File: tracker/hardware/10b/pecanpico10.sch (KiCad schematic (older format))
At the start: 121 parts, among them IC1 SPV1040T, IC10 AS213-92LF, IC2 TPS62260DRVR, IC3 ADP322ACPZ-115-R7, IC4 Si4464-B1B-FM, IC5 STM32F413RHT6, IC6 EVA-7M or EVA-M8, IC7 PAC1720-1-AIA-TR, IC8 TPS62260DRVR, IC9 BME280, J1 DM3AT-SF-PEJM5, J2 CONN_01X15, P1 CONN_01X25, P3 ZX62-B-5PA(33), P4 SMA, Q1 FDN306P, X1 KT2016K26000BCW18ZAS

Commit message: Fixed USB/battery isolation bug, increased schottky diode pad size
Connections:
- net +BATT: now also Q1.2 (S)
- net BATT_CONN: no longer names the net of J2.3 (P3), W11.1
- net BATT_CONN: no longer Q1.2 (S)
- net IO_RXD renamed IO_RXD_SDA
- net IO_TXD renamed IO_TXD_SCL
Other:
- note added: "Conect solar cells\nbetween pin 1 and 2"
- note added: "Connect pin 13 and 14 to get\ninto the STM bootloader"
- note added: "Connect pin 3 and 4 with a\njumper in order to connect\nthe battery with the circuit"
- note added: "Pin 12: Pin for general purpose"
- note added: "Pin 6 and 7 can be either\nused for UART or I2C"
- note added: "Pin 8-11: SWD interface"
- note added: "Solder the battery\nto those pads\n(either LiPO or\n3x L92 batteries)"
- moved on the sheet: D1, J2, Q1, R16, R31, W1, W10, W11

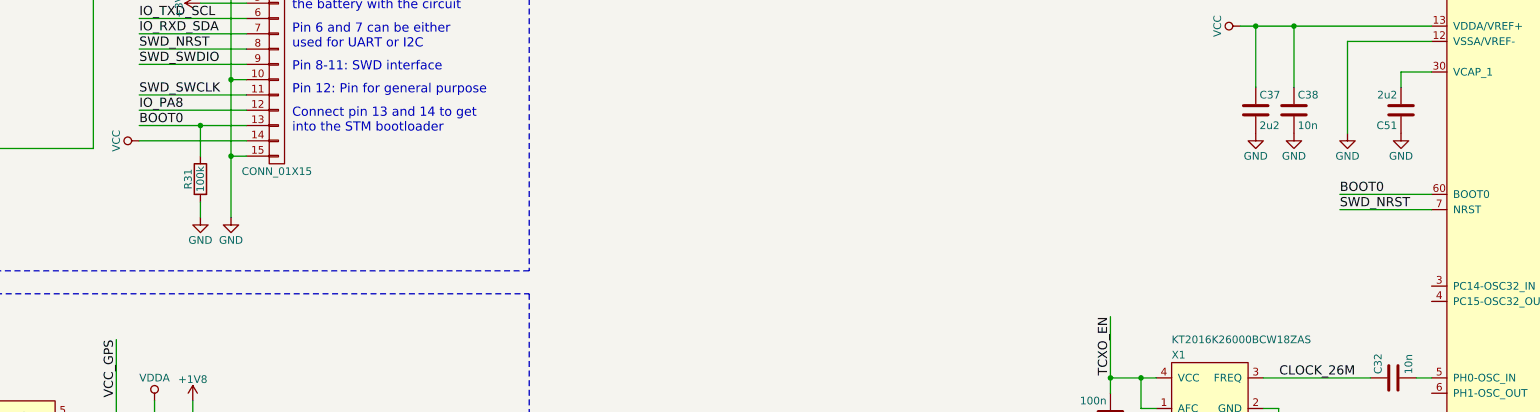
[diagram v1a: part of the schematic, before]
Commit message: Added one more pin to pinheader
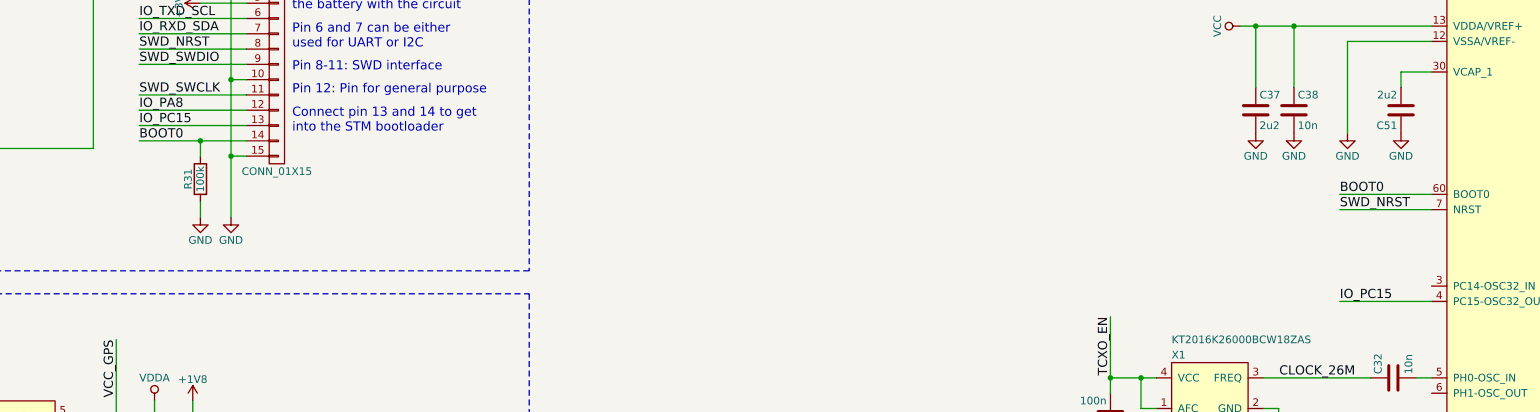
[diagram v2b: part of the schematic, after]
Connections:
- net BOOT0: now also J2.14 (P14); no longer J2.13 (P13)
- net VCC: no longer J2.14 (P14)
- net IO_PC15: now reaches IC5.4 (PC15-OSC32_OUT)
- net IO_PC15: now also J2.13 (P13)
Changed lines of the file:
@@
 Text Label 15800 5100 0    60   ~ 0
 BOOT0
-Text Label 7950 4650 0    60   ~ 0
+Text Label 7950 4750 0    60   ~ 0
 BOOT0
 $Comp
@@
 	1    0    0    -1
 $EndComp
-$Comp
-L VCC #PWR0102
-U 1 1 5A304A3C
-P 7950 4750
-F 0 "#PWR0102" H 7950 4600 50  0001 C CNN
-F 1 "VCC" H 7950 4900 50  0000 C CNN
-F 2 "" H 7950 4750 50  0001 C CNN
-F 3 "" H 7950 4750 50  0001 C CNN
-	1    7950 4750
-	0    -1   -1   0
-$EndComp
 Text Notes 1300 8050 0    60   ~ 0
 Power and Voltage sensing
 $Comp
-L +3V3 #PWR0103
+L +3V3 #PWR0102
 U 1 1 5A319E64
 P 14350 14150
-F 0 "#PWR0103" H 14350 14000 50  0001 C CNN
+F 0 "#PWR0102" H 14350 14000 50  0001 C CNN
 F 1 "+3V3" H 14350 14290 50  0000 C CNN
 F 2 "" H 14350 14150 50  0000 C CNN
@@
 $EndComp
 $Comp
-L +1V8 #PWR0104
+L +1V8 #PWR0103
 U 1 1 5A31B091
 P 11900 14000
-F 0 "#PWR0104" H 11900 13850 50  0001 C CNN
+F 0 "#PWR0103" H 11900 13850 50  0001 C CNN
 F 1 "+1V8" H 11900 14140 50  0000 C CNN
 F 2 "" H 11900 14000 50  0001 C CNN
@@
 $EndComp
 $Comp
-L +1V8 #PWR0105
+L +1V8 #PWR0104
 U 1 1 5A31B20B
 P 8300 6450
-F 0 "#PWR0105" H 8300 6300 50  0001 C CNN
+F 0 "#PWR0104" H 8300 6300 50  0001 C CNN
 F 1 "+1V8" H 8300 6590 50  0000 C CNN
 F 2 "" H 8300 6450 50  0001 C CNN
@@
 POWER BUSSES
 $Comp
-L VCC #PWR0106
+L VCC #PWR0105
 U 1 1 5A328681
 P 5900 3150
-F 0 "#PWR0106" H 5900 3000 50  0001 C CNN
+F 0 "#PWR0105" H 5900 3000 50  0001 C CNN
 F 1 "VCC" H 5900 3300 50  0000 C CNN
 F 2 "" H 5900 3150 50  0001 C CNN
@@
 $EndComp
 $Comp
-L GND #PWR0107
+L GND #PWR0106
 U 1 1 5A319B63
 P 9150 15050
-F 0 "#PWR0107" H 9150 14800 50  0001 C CNN
+F 0 "#PWR0106" H 9150 14800 50  0001 C CNN
 F 1 "GND" H 9150 14900 50  0000 C CNN
 F 2 "" H 9150 15050 50  0000 C CNN
@@
 $EndComp
 $Comp
-L GND #PWR0108
+L GND #PWR0107
 U 1 1 5A318389
 P 20100 7750
-F 0 "#PWR0108" H 20100 7500 50  0001 C CNN
+F 0 "#PWR0107" H 20100 7500 50  0001 C CNN
 F 1 "GND" H 20100 7600 50  0000 C CNN
 F 2 "" H 20100 7750 50  0001 C CNN
@@
 TCXO_EN
 $Comp
-L GND #PWR0109
+L GND #PWR0108
 U 1 1 5A3CF6C1
 P 7300 3650
-F 0 "#PWR0109" H 7300 3400 50  0001 C CNN
+F 0 "#PWR0108" H 7300 3400 50  0001 C CNN
 F 1 "GND" H 7300 3500 50  0000 C CNN
 F 2 "" H 7300 3650 50  0000 C CNN
@@
 	11900 12900 12900 12900
 Wire Wire Line
-	7950 4750 8650 4750
-Wire Wire Line
 	8450 3750 8650 3750
 Wire Wire Line
@@
 	18600 6750 19800 6750
 Wire Wire Line
-	7950 4650 8650 4650
-Wire Wire Line
 	6000 3150 5900 3150
 Wire Wire Line
@@
 Wire Wire Line
 	2800 12900 3500 12900
-Wire Wire Line
-	8350 4850 8350 4650
-Connection ~ 8350 4650
 Wire Wire Line
 	8350 5250 8350 5150
@@
 $EndComp
 $Comp
-L +BATT #PWR?
+L +BATT #PWR0109
 U 1 1 5AD41EDF
 P 7500 2600
-F 0 "#PWR?" H 7500 2450 50  0001 C CNN
+F 0 "#PWR0109" H 7500 2450 50  0001 C CNN
 F 1 "+BATT" H 7500 2740 50  0000 C CNN
 F 2 "" H 7500 2600 50  0000 C CNN
@@
 Wire Notes Line
 	4800 1500 10500 1500
+Wire Wire Line
+	7950 4750 8650 4750
+Wire Wire Line
+	8650 4650 7950 4650
+Text Label 7950 4650 0    60   ~ 0
+IO_PC15
+Text Label 15800 5800 0    60   ~ 0
+IO_PC15
+Wire Wire Line
+	15800 5800 16400 5800
+Wire Wire Line
+	8350 4850 8350 4750
+Connection ~ 8350 4750
 $EndSCHEMATC

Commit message: Relabeled pinheader
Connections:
- net IO_RXD_SDA renamed IO_RXD
- net IO_TXD_SCL renamed IO_TXD

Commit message: Fixed power measuring bug
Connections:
- net +BATT: no longer IC7.3 (SENSE2+), R22.1, R29.2
- net VDD: now also IC7.3 (SENSE2+), R22.1, R29.2; no longer C3.1, C4.2, C7.2, C8.1, C9.1, IC1.4 (VOUT), IC2.4 (EN), IC2.5 (VIN), IC3.10 (VIN3), IC3.2 (VBIAS), IC3.3 (VIN1/VIN2), IC7.4 (SENSE2-), IC8.4 (EN), IC8.5 (VIN), R1.1, R22.2, R30.2, R5.1
- new net SENSE_BAT-: C3.1, C4.2, C7.2, C8.1, C9.1, IC1.4 (VOUT), IC2.4 (EN), IC2.5 (VIN), IC3.10 (VIN3), IC3.2 (VBIAS), IC3.3 (VIN1/VIN2), IC7.4 (SENSE2-), IC8.4 (EN), IC8.5 (VIN), R1.1, R22.2, R30.2, R5.1
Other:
- moved on the sheet: C10, C11, C12, C8, C9, D4, IC3, R14, R15, R9

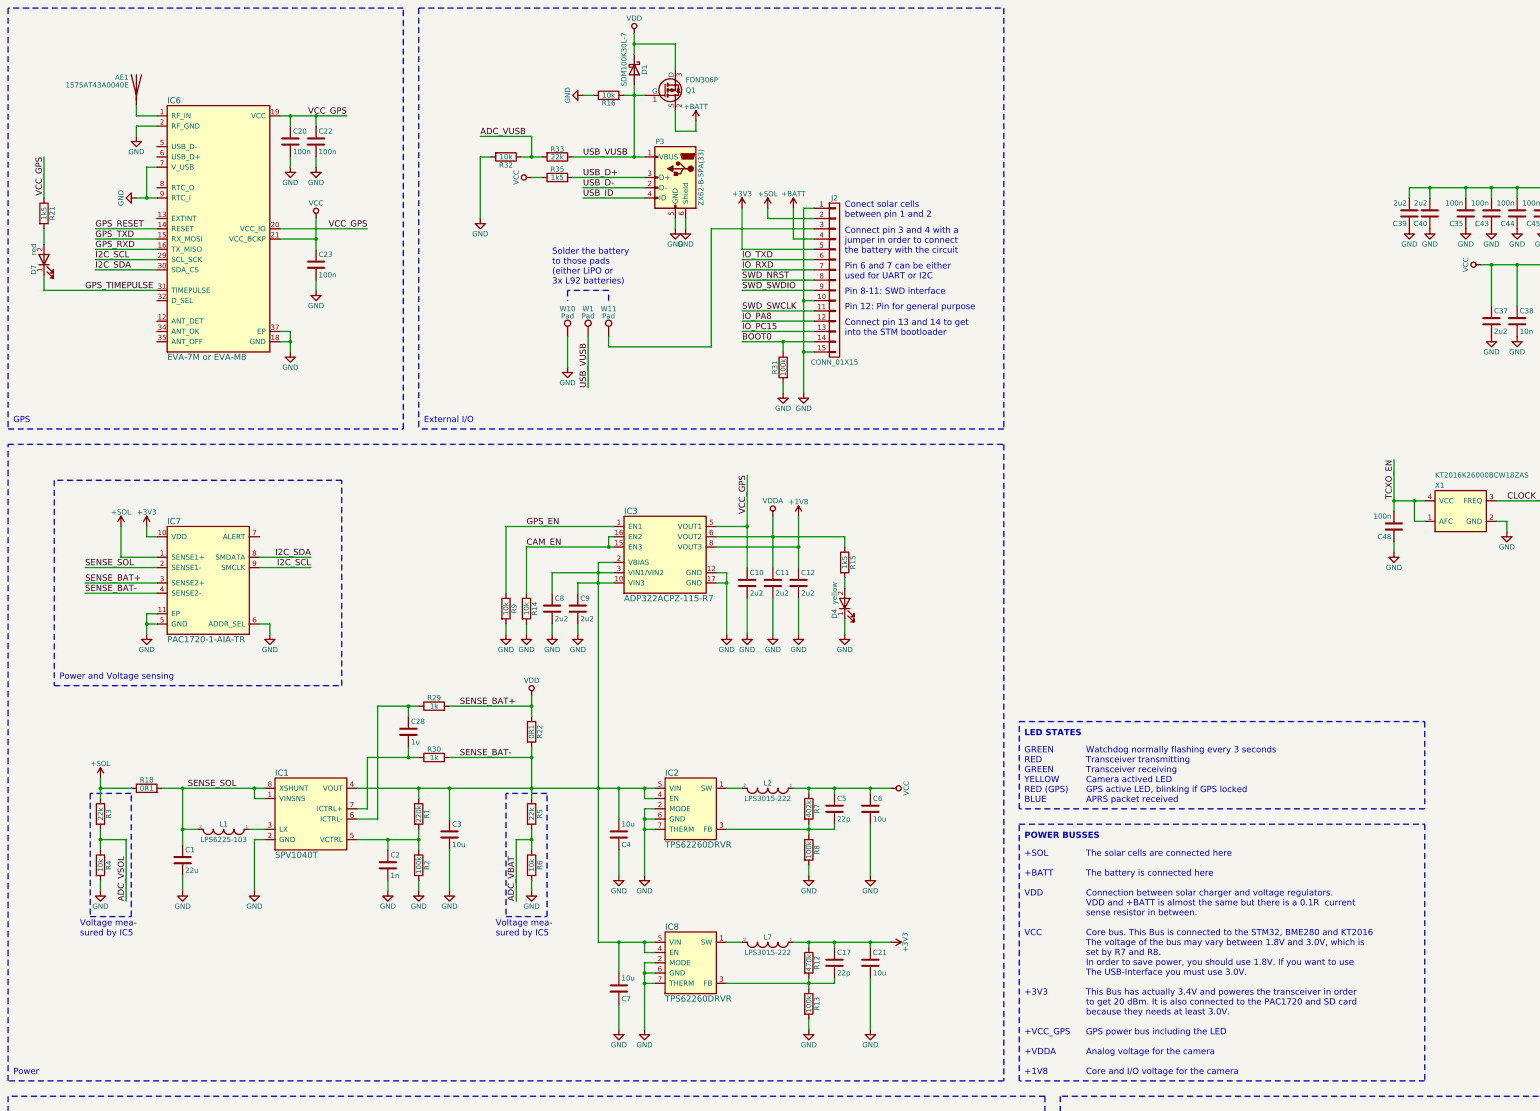
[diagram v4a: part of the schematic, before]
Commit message: Added 2m bandpass trap filter in GPS rx Removed unnecessary resistor Edited/Added schematic comments
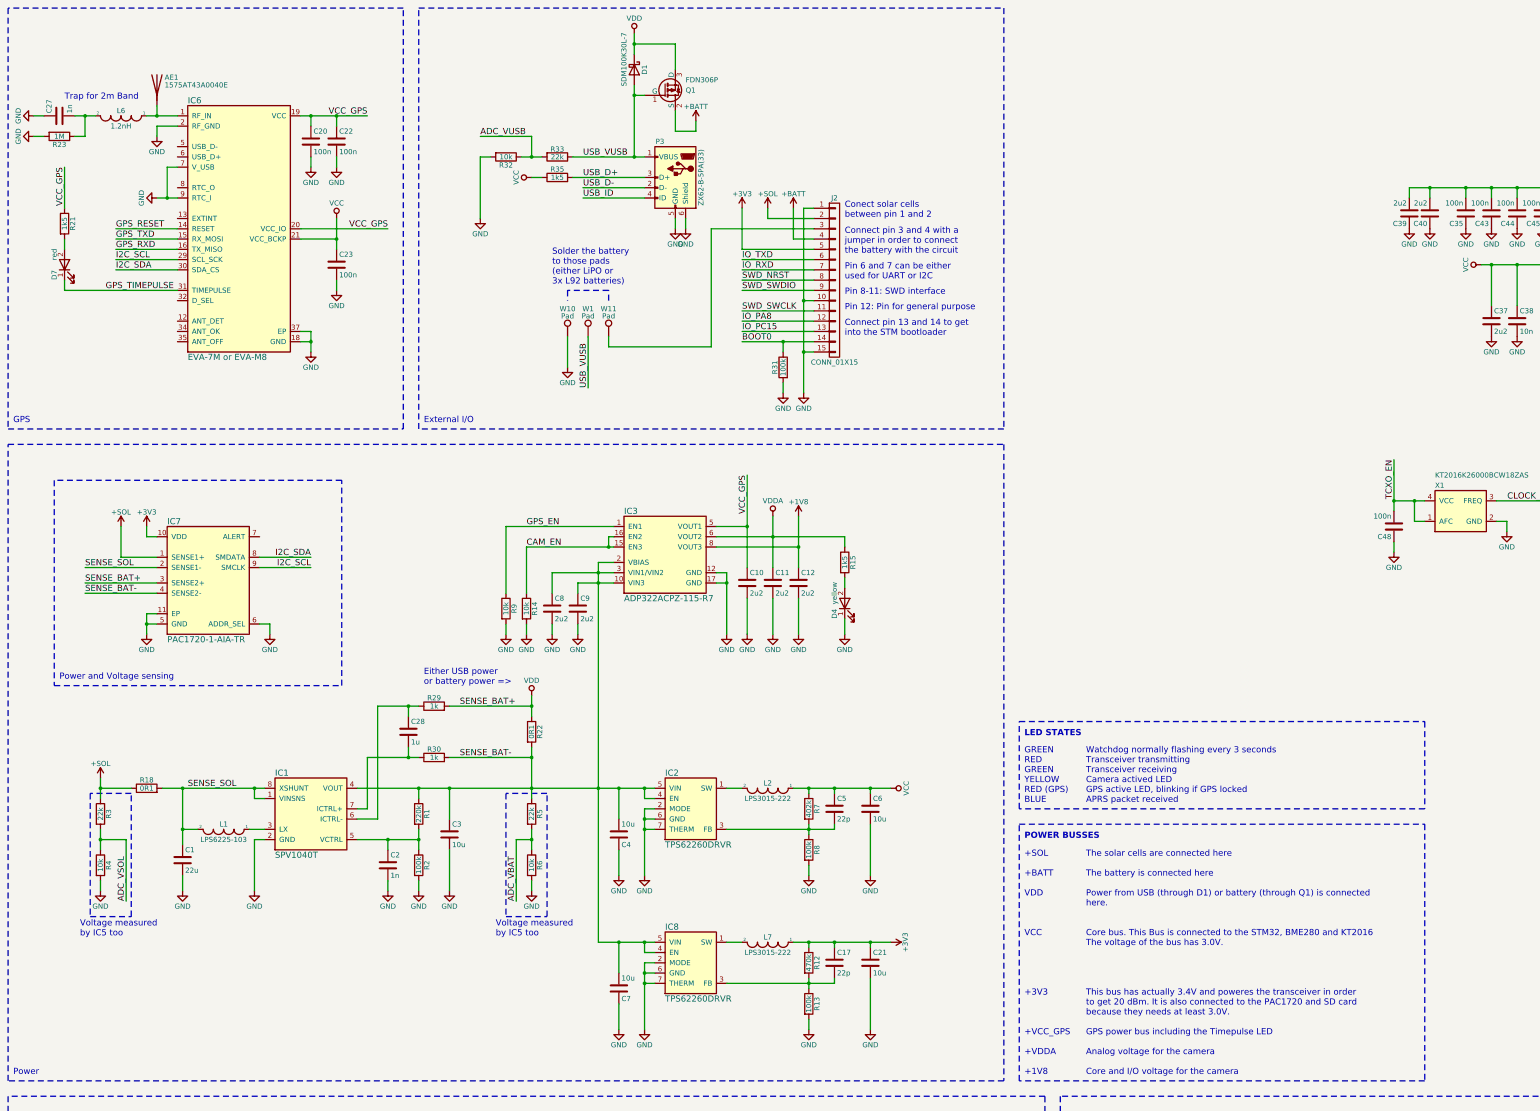
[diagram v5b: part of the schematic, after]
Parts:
- removed R16: 10k, pecanpico:R_0402, symbol R
- added C27: 1n, pecanpico:C_0402, symbol C
- added L6: 1.2nH, pecanpico:R_0603, symbol INDUCTOR
- added R23: 1M, pecanpico:R_0402, symbol R
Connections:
- net GND: now also C27.1, R23.2
- net at AE1.1 (A), IC6.1 (RF_IN): now also L6.1
- new net: C27.2, L6.2, R23.1
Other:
- note added: "Either USB power\nor battery power =>"
- note added: "The solar cells are connected here\n\nThe battery is connected here\n\nPower from USB (through D1) or battery (through Q1) is connected\nhere.\n\n\nCore bus. This Bus is connected to the STM32, BME280 and KT2016\nThe voltage of the bus has 3.0V.\n\n\n\n\nThis bus has actually 3.4V and poweres the transceiver in order\nto get 20 dBm. It is also connected to the PAC1720 and SD card\nbecause they ne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"
- note added: "Trap for 2m Band"
- note added: "Voltage measured\nby IC5 too"
- note removed: "The solar cells are connected here\n\nThe battery is connected here\n\nConnection between solar charger and voltage regulators.\nVDD and +BATT is almost the same but there is a 0.1R current\nsense resistor in between.\n\nCore bus. This Bus is connected to the STM32, BME280 and KT2016\nThe voltage of the bus may vary between 1.8V and 3.0V, which is\nset by R7 and R8.\nIn order to save power, you s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"
- note removed: "Voltage mea-\nsured by IC5"
- moved on the sheet: AE1, C20, C22, C23, D7, IC6, R21

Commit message: Added SAW Filter Optimized Antenna connections Created SAW Filter pad
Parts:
- removed C22, C23: 100n, pecanpico:C_0402, symbol C
- removed C27: 1n, pecanpico:C_0402, symbol C
- removed L6: 1.2nH, pecanpico:R_0603, symbol INDUCTOR
- removed R23: 1M, pecanpico:R_0402, symbol R
- added X2: SF2316H, pecanpico:tcxo, symbol SAW
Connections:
- net CAM_VSYNC: now also IC5.35 (PB14); no longer IC5.25 (PC5)
- net GND: now also X2.2 (GND), X2.4 (GND); no longer P1.25 (P25)
- net GPS_EN: now also IC5.25 (PC5); no longer IC5.50 (PA15)
- net GPS_RESET: now also IC5.50 (PA15); no longer IC5.35 (PB14)
- net GPS_TIMEPULSE: now also R21.2; no longer D7.1 (K)
- net IO_PA8: now also J2.13 (P13); no longer J2.12 (P12)
- net IO_PC15: now also J2.12 (P12); no longer J2.13 (P13)
- net VCC_GPS: now also D7.2 (A); no longer R21.1
- net at IC6.1 (RF_IN): now also X2.3 (OUT); no longer AE1.1 (A)
- new net: D7.1 (K), R21.1
- new net: AE1.1 (A), X2.1 (IN)
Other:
- note removed: "Trap for 2m Band"
- moved on the sheet: AE1, C20, D7, IC6, R21

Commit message: Renamed power nets, added comments to schematic, exported schematic and 3D pictures to PDF
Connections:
- net labels added: +3V0, +GPS, +TCXO
- net labels removed: TCXO_EN, VCC, VCC_GPS
- wire segments 426 -> 428
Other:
- note added: "Connect pin 5 and 14 to get\ninto the STM bootloader"
- note added: "Exact voltage: 3.01V\nPowers: STM32, BME280"
- note added: "Exact voltage: 3.42V\nPowers: Si4464, SD card\n PAC1720"
- note added: "Pin 12 and 13 is supposed to\nbe used as I2C (bitbang)"
- note added: "Pin 6 and 7 is supposed to\nbe used as UART"
- note added: "There are multiple ways to power the PCB\n- Solar only: In this case, the SPV1040 will boost the\n voltage to 4.1V (VBAT). VBAT will be used to power\n the circuit.\n- Solar and LiPO: The SPV1040 will charge the LiPO\n until 4.1V (VBAT). The LiPO will power the circuit.\n- USB only: The USB voltage is fed directly into the\n TPS62260's and LDO without using the SPV1040.\n- USB and battery (pri & 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"
- note removed: "Connect pin 13 and 14 to get\ninto the STM bootloader"
- note removed: "Pin 12: Pin for general purpose"
- note removed: "Pin 6 and 7 can be either\nused for UART or I2C"
- moved on the sheet: C1, C10, C11, C12, C17, C2, C21, C28, C3, C4, C5, C6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
